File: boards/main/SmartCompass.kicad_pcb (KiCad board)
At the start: 4 copper layers, 70 x 70 mm, 0 parts

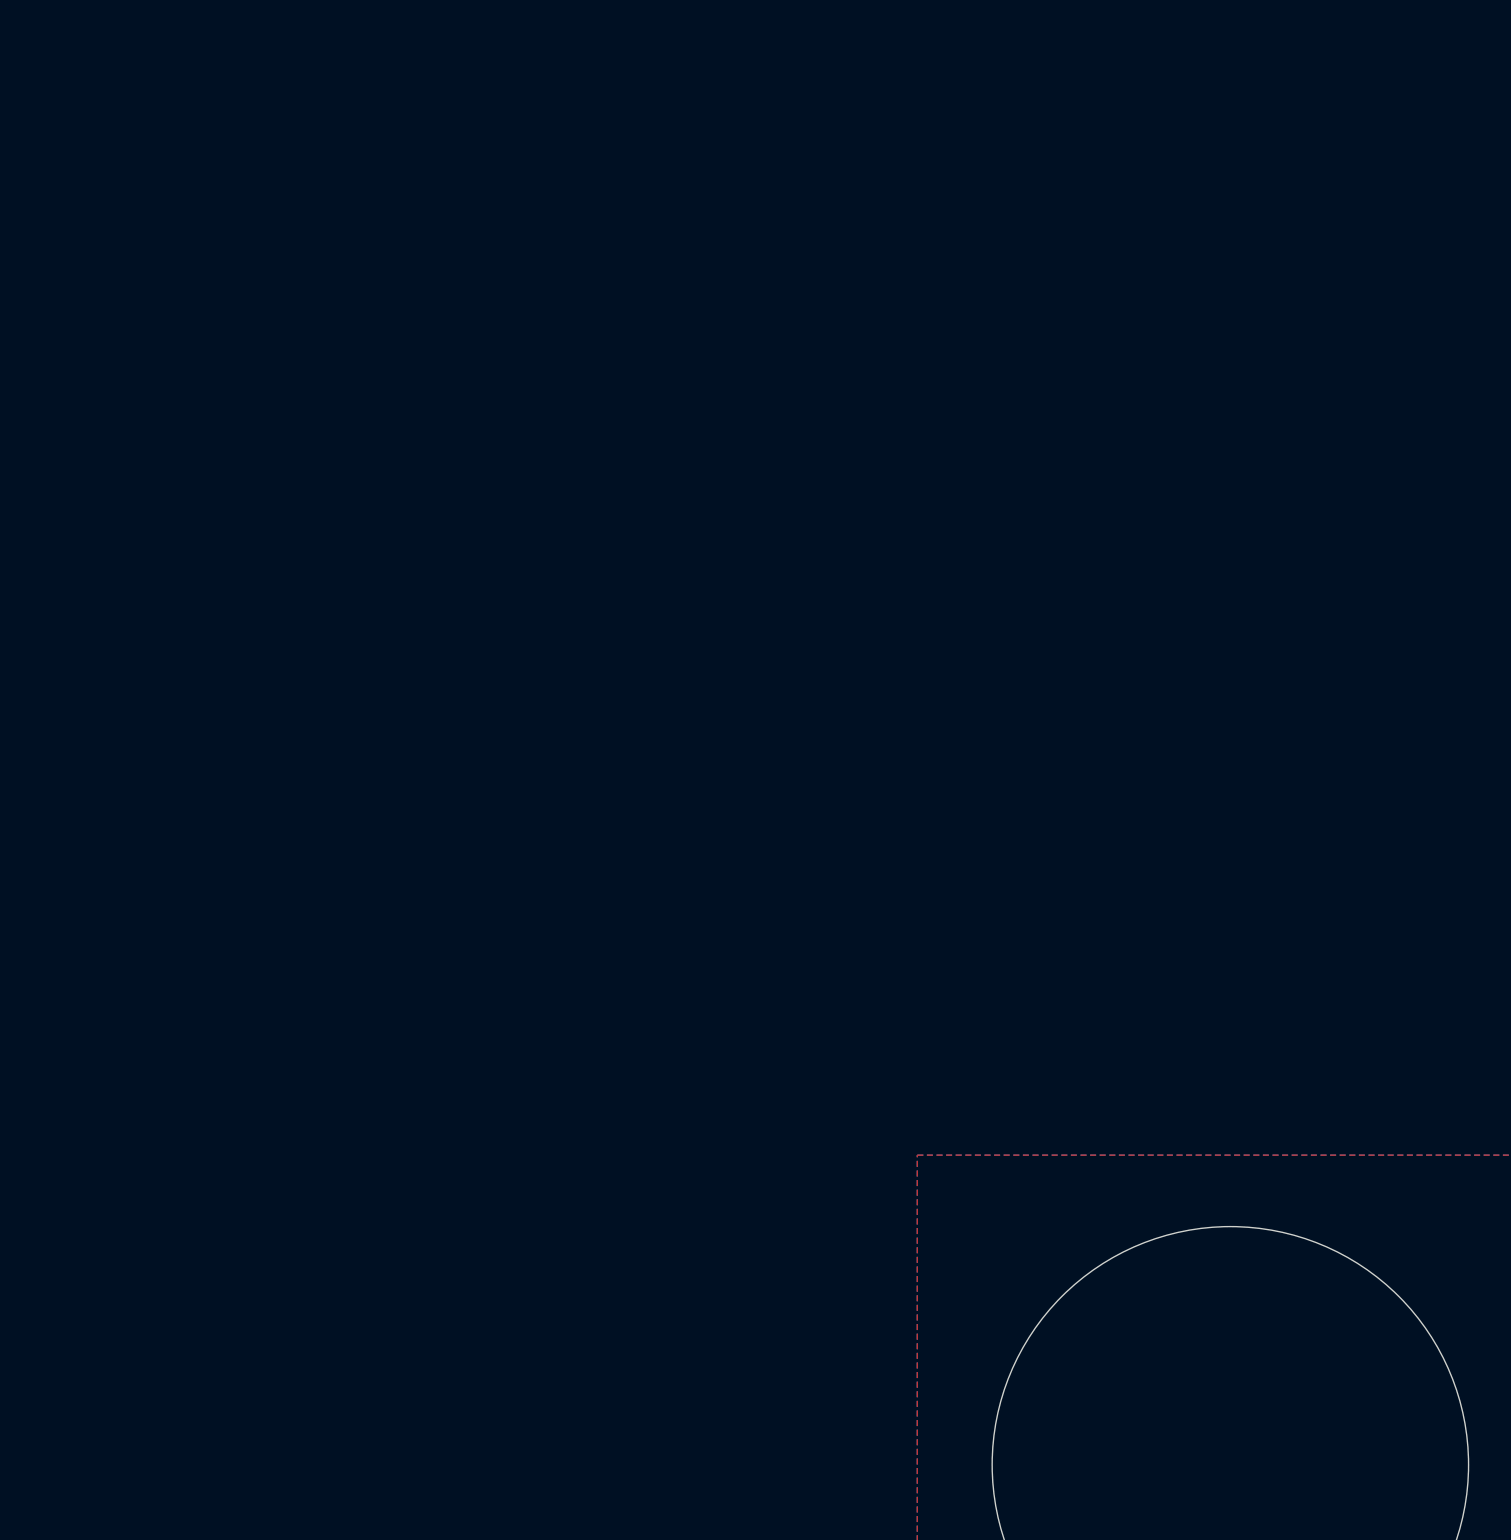
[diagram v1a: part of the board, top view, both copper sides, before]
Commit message: Initial placements of main board components. Also set some trace rules
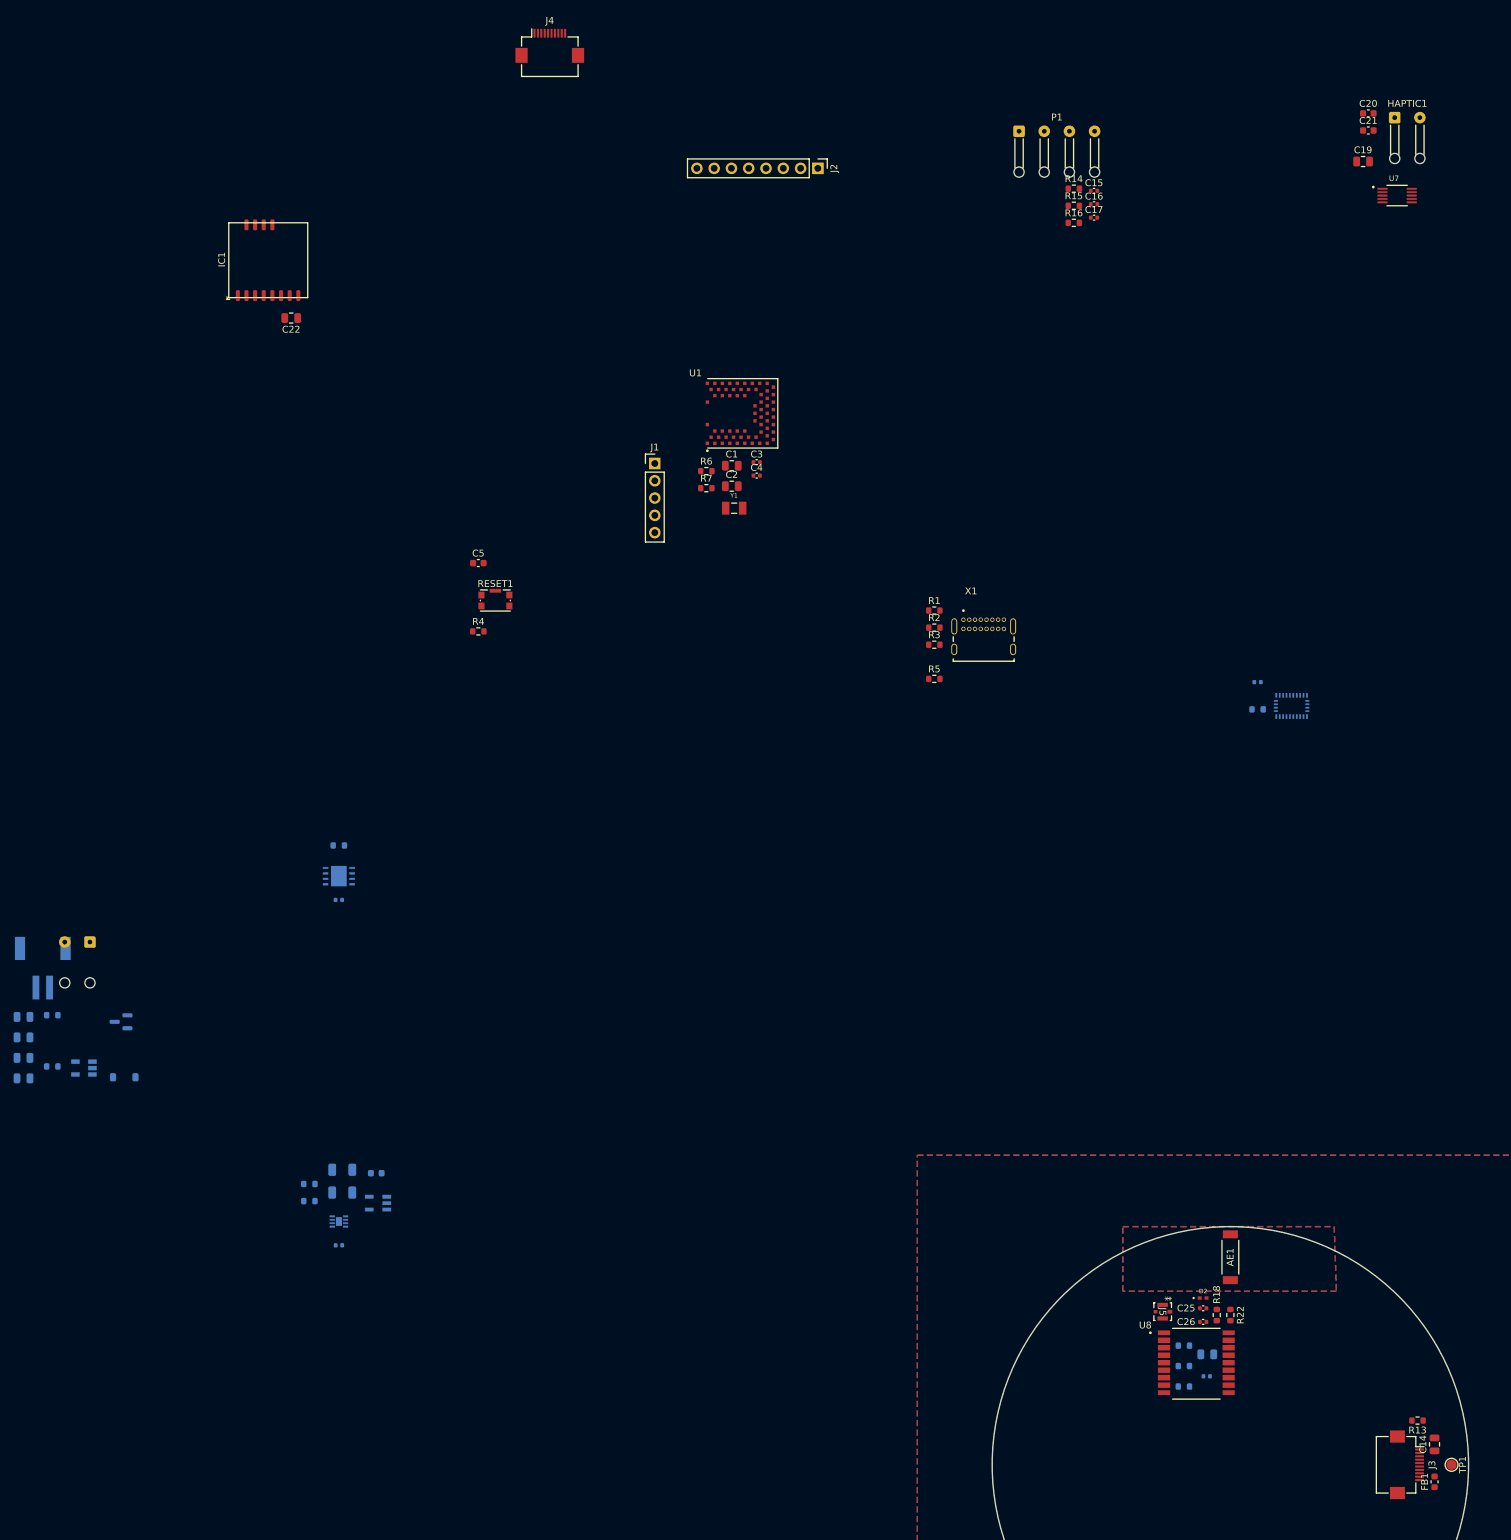
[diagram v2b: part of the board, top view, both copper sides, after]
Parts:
- added AE1: 1575AT43A0040001E, smart_compass:ANT_1575AT_JOT, F.Cu at (100.0, 69.5)
- added BATT1: JST_PH, smart_compass:JST_S2B-PH-SM4-TB, B.Cu at (-74.5, 29.9)
- added C1: 10uF, Capacitor_SMD:C_0805_2012Metric, F.Cu at (26.7, -46.8)
- added C10: 10uF, Capacitor_SMD:C_0805_2012Metric, B.Cu at (-77.3, 40.2)
- added C11: 4.7uF, Capacitor_SMD:C_1206_3216Metric, B.Cu at (-30.5, 60.0)
- added C12: 10uF, Capacitor_SMD:C_0805_2012Metric, B.Cu at (-77.3, 43.2)
- added C13: 0.1uF, Capacitor_SMD:C_0402_1005Metric, B.Cu at (-31.0, 67.8)
- added C14: 22uF, Capacitor_SMD:C_0805_2012Metric, F.Cu at (130.0, 97.0)
- added C15: 0.1uF, Capacitor_SMD:C_0402_1005Metric, F.Cu at (80.0, -87.2)
- added C16: 0.1uF, Capacitor_SMD:C_0402_1005Metric, F.Cu at (80.0, -85.2)
- added C17: 0.1uF, Capacitor_SMD:C_0402_1005Metric, F.Cu at (80.0, -83.2)
- added C18: 0.1uF, Capacitor_SMD:C_0402_1005Metric, B.Cu at (104.0, -15.0)
- added C19: 10uF, Capacitor_SMD:C_0805_2012Metric, F.Cu at (119.5, -91.5)
- added C2: 10uF, Capacitor_SMD:C_0805_2012Metric, F.Cu at (26.7, -43.8)
- added C20: 1uF, Capacitor_SMD:C_0603_1608Metric, F.Cu at (120.3, -98.6)
- added C21: 1uF, Capacitor_SMD:C_0603_1608Metric, F.Cu at (120.3, -96.1)
- added C22: 10uF, Capacitor_SMD:C_0805_2012Metric, F.Cu at (-38.0, -68.5)
- added C23: 0.1uF, Capacitor_SMD:C_0402_1005Metric, B.Cu at (96.5, 87.0)
- added C24: 10uF, Capacitor_SMD:C_0805_2012Metric, B.Cu at (96.6, 83.8)
- added C25: NM, Capacitor_SMD:C_0402_1005Metric, F.Cu at (96.0, 77.0)
- added C26: NM, Capacitor_SMD:C_0402_1005Metric, F.Cu at (96.0, 79.0)
- added C3: 12pF, Capacitor_SMD:C_0402_1005Metric, F.Cu at (30.4, -47.3)
- added C4: 12pF, Capacitor_SMD:C_0402_1005Metric, F.Cu at (30.4, -45.4)
- added C5: 1uF, Capacitor_SMD:C_0603_1608Metric, F.Cu at (-10.5, -32.5)
- added C6: 0.1uF, Capacitor_SMD:C_0402_1005Metric, B.Cu at (-31.0, 17.0)
- added C7: 4.7uF, Capacitor_SMD:C_1206_3216Metric, B.Cu at (-30.5, 56.6)
- added C8: 10uF, Capacitor_SMD:C_0805_2012Metric, B.Cu at (-77.3, 34.2)
- added C9: 10uF, Capacitor_SMD:C_0805_2012Metric, B.Cu at (-77.3, 37.2)
- added CHG1: RED, LED_SMD:LED_0603_1608Metric, B.Cu at (-25.5, 57.1)
- added D1: MBR0540, Diode_SMD:D_SOD-123, B.Cu at (-62.5, 43.1)
- added D2: TPD1E05U06DPYR, smart_compass:DIO_TPD1E05U06DPYR, F.Cu at (96.0, 75.5)
- added FB1: 600R@100MHz, Inductor_SMD:L_0603_1608Metric, F.Cu at (130.0, 102.5)
- added HAPTIC1: HAPTIC_PADS, Connector_Wire:SolderWire-0.127sqmm_1x02_P3.7mm_D0.48mm_OD1mm_Relief, F.Cu at (124.2, -98.0)
- added IC1: Wio-SX1262, smart_compass:MODULE12P-1.27-11X11.6MM, F.Cu at (-47.2, -71.5)
- added J1: SWD HEADER, Connector_PinHeader_2.54mm:PinHeader_1x05_P2.54mm_Vertical, F.Cu at (15.4, -47.1)
- added J2: EXPANSION, Connector_PinHeader_2.54mm:PinHeader_1x08_P2.54mm_Vertical, F.Cu at (39.4, -90.5)
- added J3: FH12-10S-0.5SH(55), Connector_FFC-FPC:Hirose_FH12-10S-0.5SH_1x10-1MP_P0.50mm_Horizontal, F.Cu at (126.0, 100.0)
- added J4: FH12-10S-0.5SH(55), Connector_FFC-FPC:Hirose_FH12-10S-0.5SH_1x10-1MP_P0.50mm_Horizontal, F.Cu at (0.00, -108.5)
- added J5: IPEX, smart_compass:SMT_9.001E.01_TAL, F.Cu at (90.1, 77.5)
- added ONOFF1: PWRSW_PADS, Connector_Wire:SolderWire-0.127sqmm_1x02_P3.7mm_D0.48mm_OD1mm_Relief, B.Cu at (-67.6, 23.2)
- added P1: BUTTON_PADS, Connector_Wire:SolderWire-0.127sqmm_1x04_P3.7mm_D0.48mm_OD1mm_Relief, F.Cu at (69.0, -96.0)
- added Q1: DMP2045U, Package_TO_SOT_SMD:SOT-23, B.Cu at (-63.0, 34.9)
- added R1: 5.1K, Resistor_SMD:R_0603_1608Metric, F.Cu at (56.5, -25.5)
- added R10: 5.1K, Resistor_SMD:R_0603_1608Metric, B.Cu at (-35.3, 58.7)
- added R11: 3.9K, Resistor_SMD:R_0603_1608Metric, B.Cu at (-35.3, 61.2)
- added R12: 100K, Resistor_SMD:R_0603_1608Metric, B.Cu at (-73.1, 41.5)
- added R13: 500R, Resistor_SMD:R_0603_1608Metric, F.Cu at (127.5, 93.5)
- added R14: 10K, Resistor_SMD:R_0603_1608Metric, F.Cu at (77.0, -87.5)
- added R15: 10K, Resistor_SMD:R_0603_1608Metric, F.Cu at (77.0, -85.0)
- added R16: 10K, Resistor_SMD:R_0603_1608Metric, F.Cu at (77.0, -82.5)
- added R17: 10K, Resistor_SMD:R_0603_1608Metric, B.Cu at (104.0, -11.0)
- added R18: NM, Resistor_SMD:R_0603_1608Metric, F.Cu at (98.0, 78.0)
- added R19: 100K, Resistor_SMD:R_0603_1608Metric, B.Cu at (93.2, 82.5)
- added R2: 5.1K, Resistor_SMD:R_0603_1608Metric, F.Cu at (56.5, -23.0)
- added R20: 1K, Resistor_SMD:R_0603_1608Metric, B.Cu at (93.2, 85.5)
- added R21: 1K, Resistor_SMD:R_0603_1608Metric, B.Cu at (93.2, 88.5)
- added R22: 0R, Resistor_SMD:R_0603_1608Metric, F.Cu at (100.0, 78.0)
- added R3: 27R, Resistor_SMD:R_0603_1608Metric, F.Cu at (56.5, -20.5)
- added R4: 5.1K, Resistor_SMD:R_0603_1608Metric, F.Cu at (-10.5, -22.5)
- added R5: 27R, Resistor_SMD:R_0603_1608Metric, F.Cu at (56.5, -15.5)
- added R6: 4.7K, Resistor_SMD:R_0603_1608Metric, F.Cu at (23.0, -46.0)
- added R7: 4.7K, Resistor_SMD:R_0603_1608Metric, F.Cu at (23.0, -43.5)
- added R8: 10K, Resistor_SMD:R_0603_1608Metric, B.Cu at (-31.0, 9.00)
- added R9: 100K, Resistor_SMD:R_0603_1608Metric, B.Cu at (-73.1, 33.9)
- added RESET1: KMR2, Button_Switch_SMD:SW_Push_1P1T-SH_NO_CK_KMR2xxG, F.Cu at (-8.00, -27.0)
- added TP1: TestPoint, TestPoint:TestPoint_Pad_D1.5mm, F.Cu at (132.5, 100.0)
- added U1: BMD-340-A-R, smart_compass:RIGADO_BMD-340-A-R, F.Cu at (26.0, -54.5)
- added U2: S25FL064LABNFI043, smart_compass:SON80P400X400X60-9N, B.Cu at (-31.0, 13.5)
- added U3: RT9080-33GJ5, smart_compass:SOT94P280X100-5N, B.Cu at (-68.5, 41.7)
- added U4: MCP73831T-2ACI_OT, smart_compass:SOT95P280X145-5N, B.Cu at (-25.2, 61.6)
- added U5: MAX17048G_T10, smart_compass:SON50P200X200X80-9N, B.Cu at (-31.0, 64.2)
- added U6: BNO086, smart_compass:IC_BNO086, B.Cu at (109.0, -11.5)
- added U7: DRV2605LDGSR, smart_compass:SOP50P490X110-10N, F.Cu at (124.5, -86.5)
- added U8: MAX-M10S-00B, smart_compass:XCVR_MAX-M10S-00B, F.Cu at (95.0, 85.0)
- added X1: USB4085-GF-A, smart_compass:GCT_USB4085-GF-A_REVA4, F.Cu at (63.8, -19.8)
- added Y1: 32.768KHZ, smart_compass:XTAL_ABS07-32.768KHZ-7-T, F.Cu at (27.1, -40.6)
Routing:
- added copper zone on B.Cu, net (none)
- added copper zone on F.Cu, net (none)
- added copper zone on In1.Cu, net (none)
- added copper zone on In2.Cu, net (none)
